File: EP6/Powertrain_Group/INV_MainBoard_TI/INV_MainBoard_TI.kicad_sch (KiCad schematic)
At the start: 30 parts, among them J1 FX26-30P-1SV, J10 CAN, J11 CAN, J12 CAN, J2 motorSense, J7 phase control monitor, J8 current, J9 CAN, Q1 2N7002, Q2 2N7002

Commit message: update INV_MainBoard_TI to V1.1
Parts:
- R3: value 20k -> 1k
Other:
- note added: "and motor temp OTP"
- note added: "aobut 50kHz"
- note added: "probably have to add filter for encoder, Isense and motor Temp considering amplify the current signal at least 2 considering adding zener to protect current signal need to add error stat indicator light maybe add more LEDs and some switches"
- moved on the sheet: C97, J10, J11, J12, J7, J9, R76

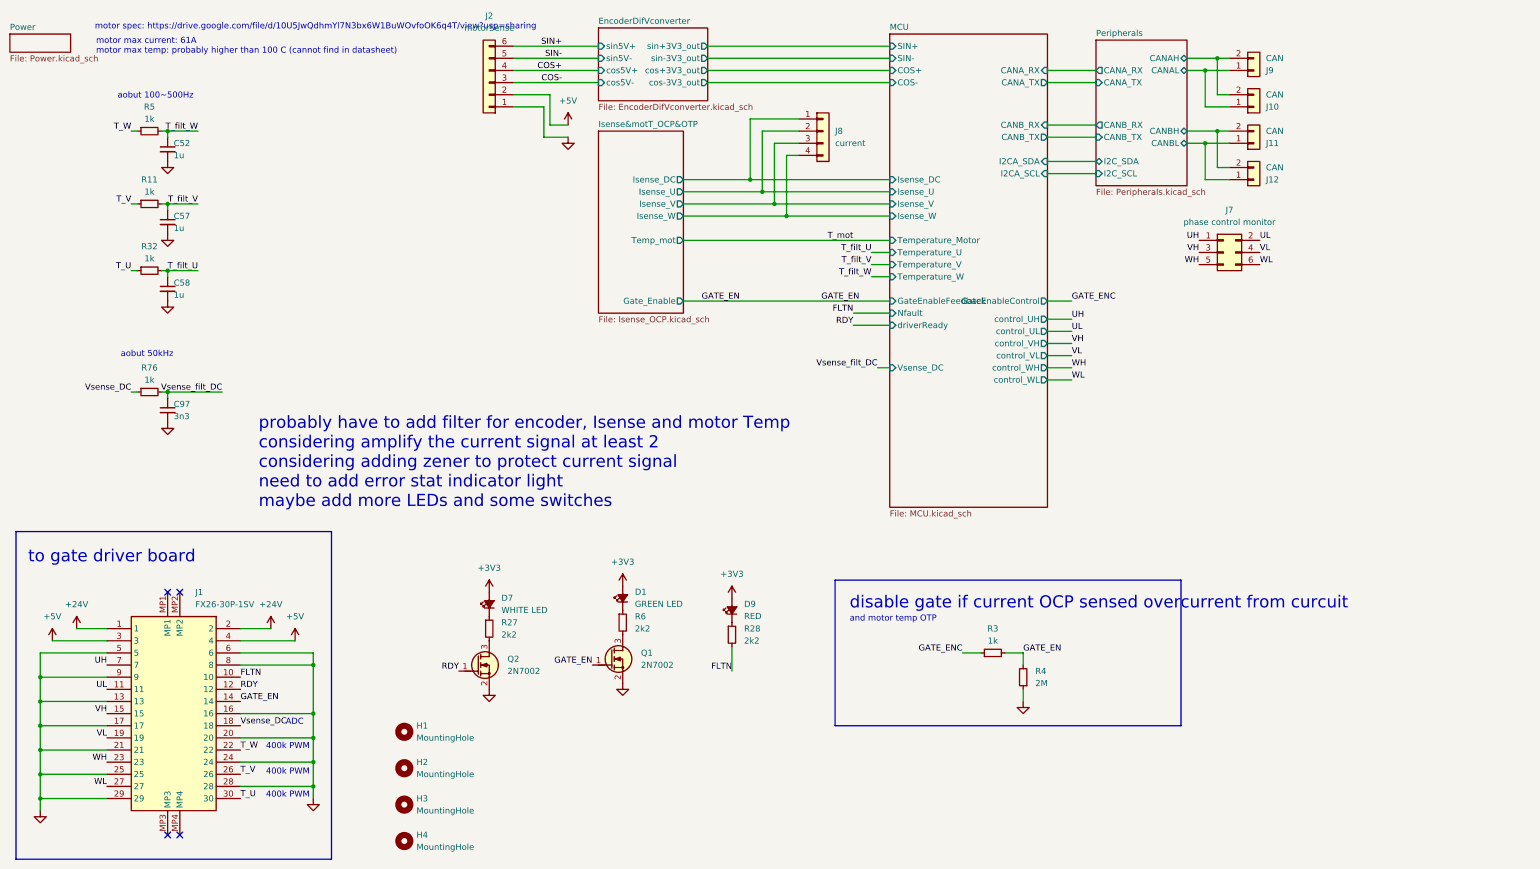
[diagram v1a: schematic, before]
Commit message: update INV_MainBoard_TI to V1.2
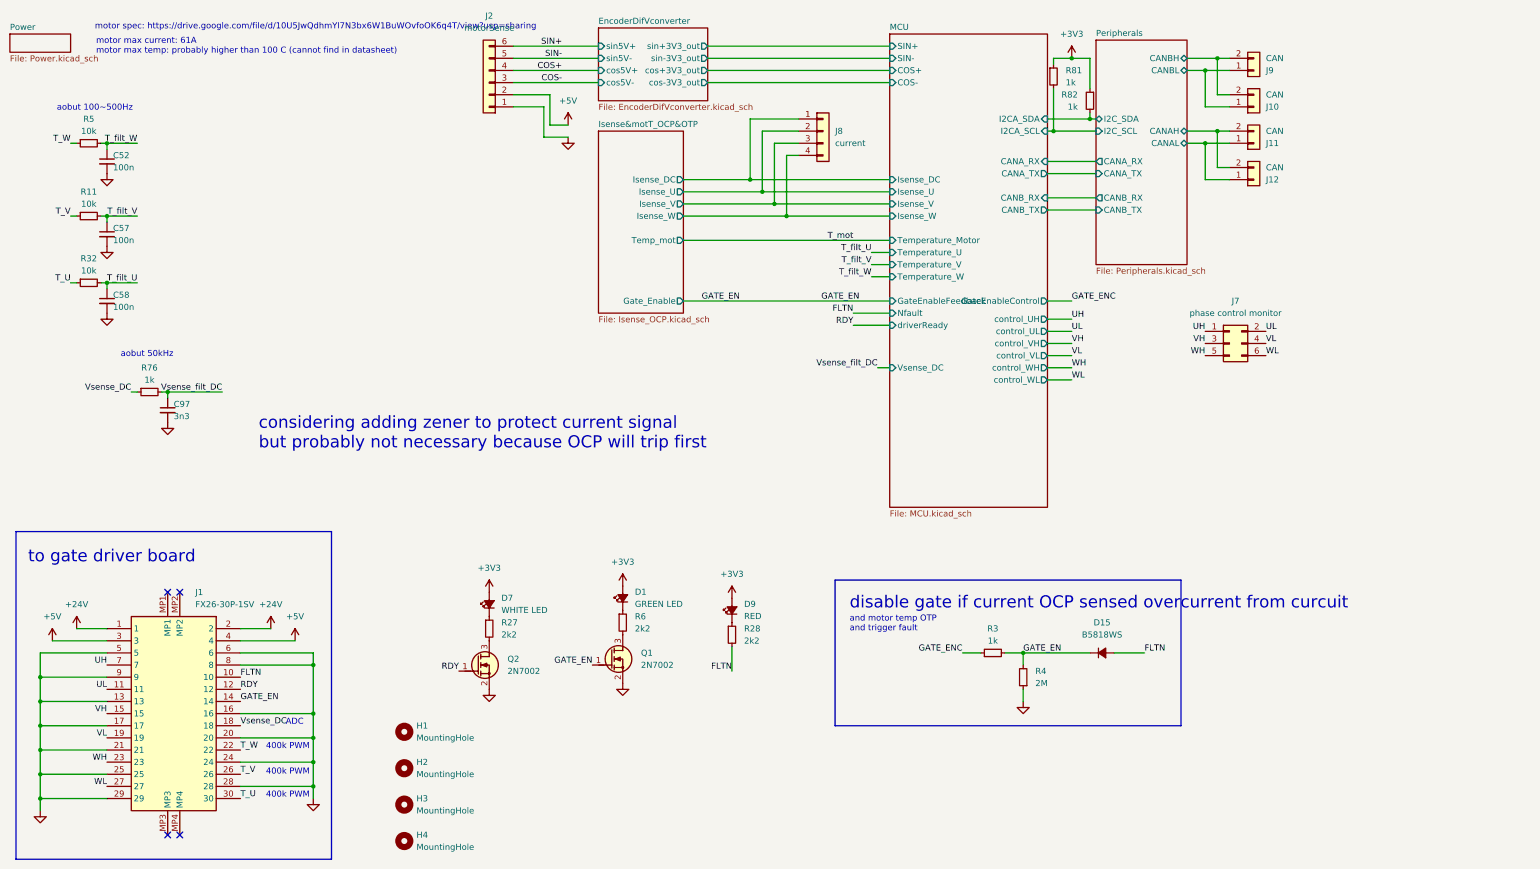
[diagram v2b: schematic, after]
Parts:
- added D15: B5818WS, Diode_SMD:D_SOD-323, symbol Device:D_Small_Filled
- added R81, R82: 1k, Resistor_SMD:R_0402_1005Metric, symbol Device:R_Small
- C52, C57, C58: value 1u -> 100n
- R11, R32, R5: value 1k -> 10k
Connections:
- net +3V3: now also R81.1, R82.1
- net FLTN: now also D15.2 (A)
- net GATE_EN: now also D15.1 (K)
- net MCU/I2CA_SCL: now also R81.2
- net MCU/I2CA_SDA: now also R82.2
- net Peripherals/CANAH: now also J11.2 (Pin_2), J12.2 (Pin_2); no longer J10.2 (Pin_2), J9.2 (Pin_2)
- net Peripherals/CANAL: now also J11.1 (Pin_1), J12.1 (Pin_1); no longer J10.1 (Pin_1), J9.1 (Pin_1)
- net Peripherals/CANBH: now also J10.2 (Pin_2), J9.2 (Pin_2); no longer J11.2 (Pin_2), J12.2 (Pin_2)
- net Peripherals/CANBL: now also J10.1 (Pin_1), J9.1 (Pin_1); no longer J11.1 (Pin_1), J12.1 (Pin_1)
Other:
- note added: "and trigger fault"
- note added: "considering adding zener to protect current signal but probably not necessary because OCP will trip first"
- note removed: "probably have to add filter for encoder, Isense and motor Temp considering amplify the current signal at least 2 considering adding zener to protect current signal need to add error stat indicator light maybe add more LEDs and some switches"
- moved on the sheet: C52, C57, C58, J7, R11, R32, R5

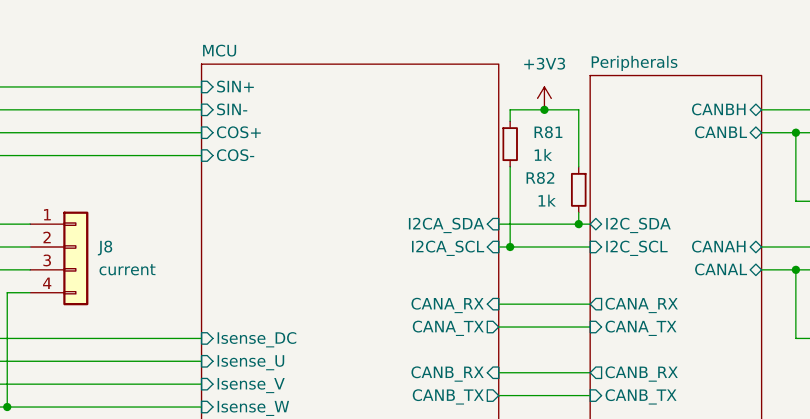
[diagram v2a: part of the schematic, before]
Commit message: update INV_MainBoard_TI to V1.3
fix negative feedback mistake in 1.65 Vref
and some other minor fix
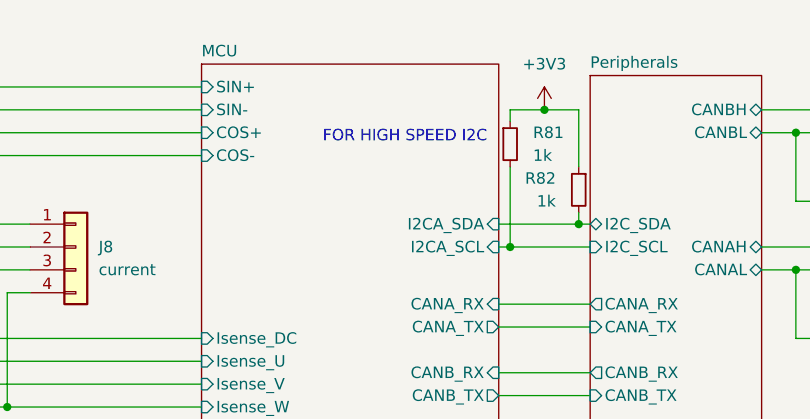
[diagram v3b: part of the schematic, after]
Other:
- note added: "FOR HIGH SPEED I2C"
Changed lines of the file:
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@@
 	(title_block
 		(title "INV_MainBoard_TI")
-		(date "2025-02-26")
-		(rev "1.2")
+		(date "2025-02-28")
+		(rev "1.3")
 		(company "NTURacing Team")
 		(comment 1 "郭哲明 Jack Kuo")
@@
 		)
 	)
+	(text "FOR HIGH SPEED I2C"
+		(exclude_from_sim no)
+		(at 221.996 25.908 0)
+		(effects
+			(font
+				(size 1.27 1.27)
+			)
+		)
+	)

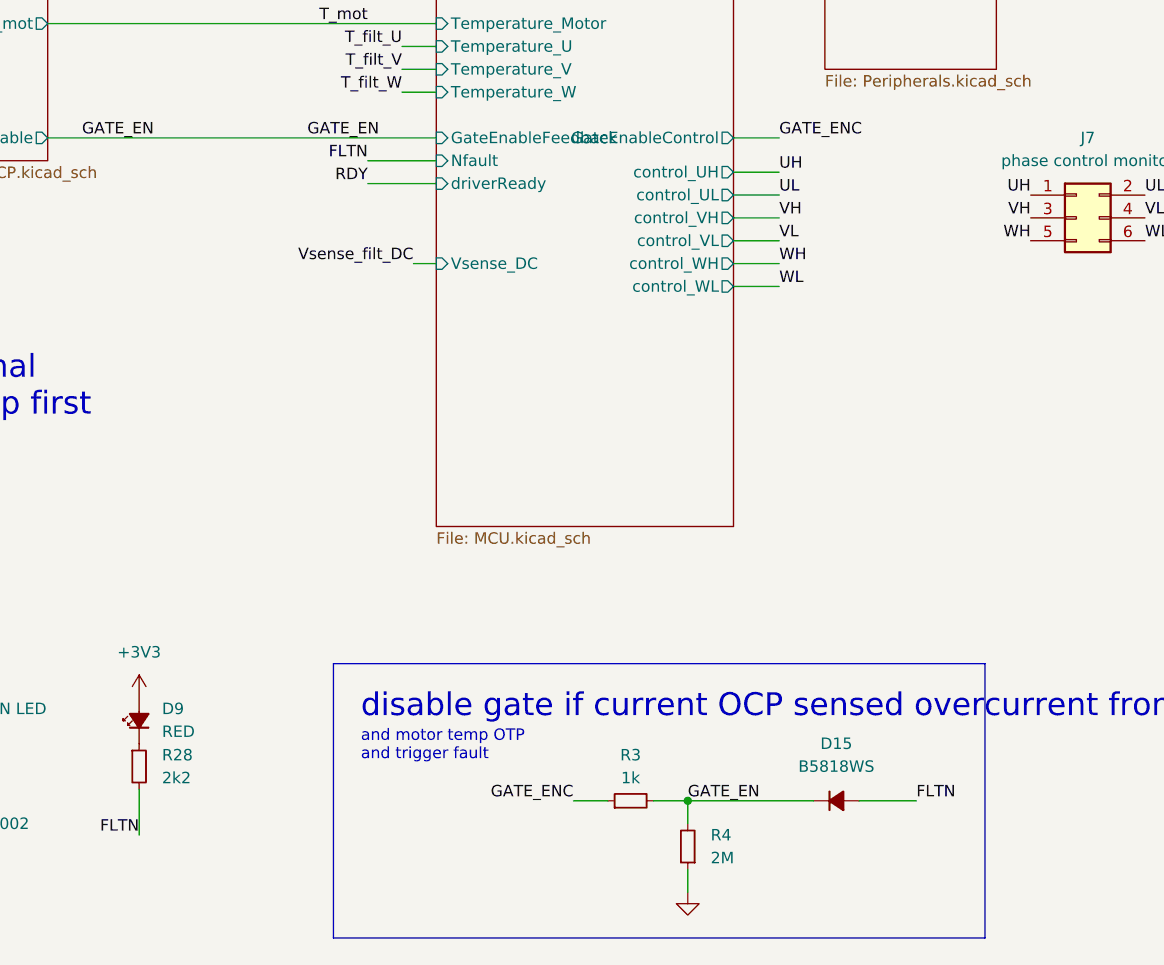
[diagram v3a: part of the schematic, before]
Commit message: update INV_MainBoard_TI to V1.4
update for JLCPCB parts
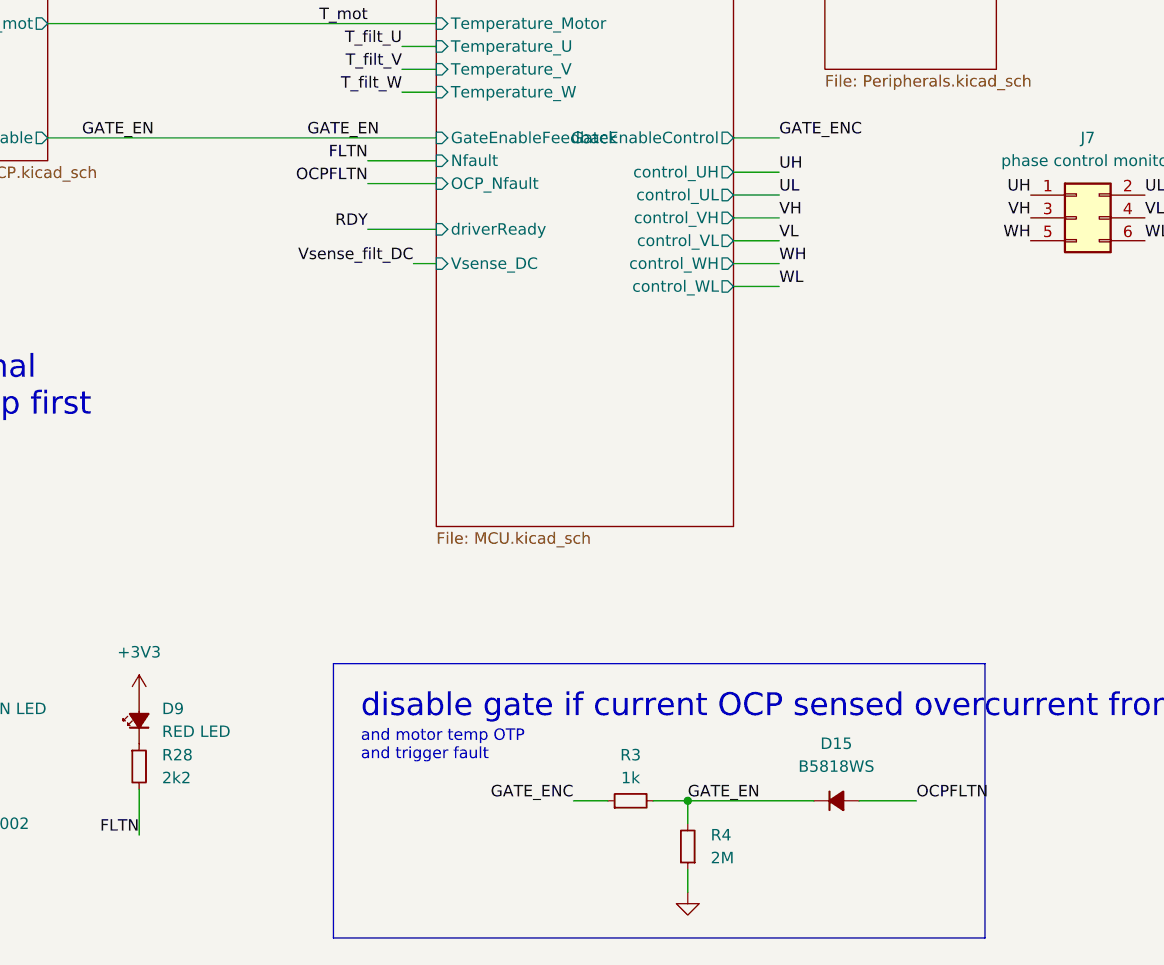
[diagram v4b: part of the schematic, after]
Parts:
- D9: value RED -> RED LED
- J1: footprint SamacSys_Parts_EP6:FX2630P1SV -> FX2630P1SV
- Q1, Q2: footprint Package_TO_SOT_SMD:SOT-23 -> PCM_Package_TO_SOT_SMD_AKL:SOT-23
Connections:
- net FLTN: no longer D15.2 (A)
- new net OCPFLTN: D15.2 (A)
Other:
- sheet MCU ports: added OCP_Nfault; removed none
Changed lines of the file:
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@@
 		(title "INV_MainBoard_TI")
 		(date "2025-02-28")
-		(rev "1.3")
+		(rev "1.4")
 		(company "NTURacing Team")
 		(comment 1 "郭哲明 Jack Kuo")
@@
 	(wire
 		(pts
+			(xy 191.77 78.74) (xy 199.39 78.74)
+		)
+		(stroke
+			(width 0)
+			(type default)
+		)
+	)
+	(wire
+		(pts
 			(xy 156.21 50.8) (xy 172.72 50.8)
 		)
@@
 	(wire
 		(pts
-			(xy 191.77 78.74) (xy 199.39 78.74)
+			(xy 191.77 83.82) (xy 199.39 83.82)
 		)
 		(stroke
@@
 		)
 	)
+	(label "OCPFLTN"
+		(at 191.77 78.74 180)
+		(effects
+			(font
+				(size 1.27 1.27)
+			)
+			(justify right bottom)
+		)
+	)
 	(label "Vsense_filt_DC"
 		(at 196.85 87.63 180)
@@
 		)
 	)
-	(label "FLTN"
+	(label "OCPFLTN"
 		(at 252.73 147.32 0)
 		(effects
@@
 	)
 	(label "RDY"
-		(at 191.77 78.74 180)
+		(at 191.77 83.82 180)
 		(effects
 			(font
@@
 			)
 		)
-		(property "Value" "RED"
+		(property "Value" "RED LED"
 			(at 168.91 139.6365 90)
 			(effects
@@
 			)
 		)
-		(property "Footprint" "SamacSys_Parts_EP6:FX2630P1SV"
+		(property "Footprint" "FX2630P1SV"
 			(at -39.04 181.61 0)
 			(effects
@@
 			)
 		)
-		(property "Footprint" "Package_TO_SOT_SMD:SOT-23"
+		(property "Footprint" "PCM_Package_TO_SOT_SMD_AKL:SOT-23"
 			(at 118.11 147.32 0)
 			(effects
@@
 			)
 		)
-		(property "Footprint" "Package_TO_SOT_SMD:SOT-23"
+		(property "Footprint" "PCM_Package_TO_SOT_SMD_AKL:SOT-23"
 			(at 146.05 146.05 0)
 			(effects
@@
 		)
 		(pin "driverReady" input
-			(at 199.39 78.74 180)
+			(at 199.39 83.82 180)
 			(effects
 				(font
@@
 			)
 		)
+		(pin "OCP_Nfault" input
+			(at 199.39 78.74 180)
+			(effects
+				(font
+					(size 1.27 1.27)
+				)
+				(justify left)
+			)
+		)
